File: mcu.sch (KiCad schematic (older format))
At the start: 26 parts, among them SW1 PTS645VL39-2, U4 CAT24C32, U5 STM32F765VIT6, X1 ECS-TXO-3225-160-TR

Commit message: Complete functional design
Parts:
- renumbered C16 to C15, C17 to C16, C18 to C17, C19 to C18, C20 to C19, C21 to C20, C22 to C21, C23 to C22, C24 to C23, C25 to C24, C26 to C25, C27 to C26, C28 to C27, C29 to C28, D33 to D6, R7 to R10, R8 to R11, R9 to R12, R125 to R9
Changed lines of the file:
@@
 $EndDescr
 $Comp
-L Device:R R9
+L Device:R R12
 U 1 1 5AD0B119
 P 10200 5950
-F 0 "R9" H 10000 5900 50  0000 L CNN
+F 0 "R12" H 10000 5900 50  0000 L CNN
 F 1 "47k" H 10000 6000 50  0000 L CNN
 F 2 "Resistor_SMD:R_0603_1608Metric" V 10130 5950 50  0001 C CNN
@@
 VDD3V3
 $Comp
-L Device:C C20
+L Device:C C19
 U 1 1 5AD085F7
 P 1800 6650
-F 0 "C20" H 1915 6696 50  0000 L CNN
+F 0 "C19" H 1915 6696 50  0000 L CNN
 F 1 "1uF" H 1915 6605 50  0000 L CNN
 F 2 "Capacitor_SMD:C_0603_1608Metric" H 1838 6500 50  0001 C CNN
@@
 $EndComp
 $Comp
-L Device:C C24
+L Device:C C23
 U 1 1 5AD086E9
 P 2200 6650
-F 0 "C24" H 2315 6696 50  0000 L CNN
+F 0 "C23" H 2315 6696 50  0000 L CNN
 F 1 "100nF" H 2315 6605 50  0000 L CNN
 F 2 "Capacitor_SMD:C_0603_1608Metric" H 2238 6500 50  0001 C CNN
@@
 VDD3V3
 $Comp
-L Device:C C19
+L Device:C C18
 U 1 1 5AD08A76
 P 1800 6250
-F 0 "C19" H 1915 6296 50  0000 L CNN
+F 0 "C18" H 1915 6296 50  0000 L CNN
 F 1 "1uF" H 1915 6205 50  0000 L CNN
 F 2 "Capacitor_SMD:C_0603_1608Metric" H 1838 6100 50  0001 C CNN
@@
 $EndComp
 $Comp
-L Device:C C23
+L Device:C C22
 U 1 1 5AD08A7D
 P 2200 6250
-F 0 "C23" H 2315 6296 50  0000 L CNN
+F 0 "C22" H 2315 6296 50  0000 L CNN
 F 1 "100nF" H 2315 6205 50  0000 L CNN
 F 2 "Capacitor_SMD:C_0603_1608Metric" H 2238 6100 50  0001 C CNN
@@
 VDD3V3
 $Comp
-L Device:C C16
+L Device:C C15
 U 1 1 5AD0945E
 P 1150 7300
-F 0 "C16" H 1265 7346 50  0000 L CNN
+F 0 "C15" H 1265 7346 50  0000 L CNN
 F 1 "100nF" H 1265 7255 50  0000 L CNN
 F 2 "Capacitor_SMD:C_0603_1608Metric" H 1188 7150 50  0001 C CNN
@@
 $EndComp
 $Comp
-L Device:C C17
+L Device:C C16
 U 1 1 5AD09C8C
 P 1600 7300
-F 0 "C17" H 1715 7346 50  0000 L CNN
+F 0 "C16" H 1715 7346 50  0000 L CNN
 F 1 "100nF" H 1715 7255 50  0000 L CNN
 F 2 "Capacitor_SMD:C_0603_1608Metric" H 1638 7150 50  0001 C CNN
@@
 $EndComp
 $Comp
-L Device:C C22
+L Device:C C21
 U 1 1 5AD09D94
 P 2050 7300
-F 0 "C22" H 2165 7346 50  0000 L CNN
+F 0 "C21" H 2165 7346 50  0000 L CNN
 F 1 "100nF" H 2165 7255 50  0000 L CNN
 F 2 "Capacitor_SMD:C_0603_1608Metric" H 2088 7150 50  0001 C CNN
@@
 $EndComp
 $Comp
-L Device:C C25
+L Device:C C24
 U 1 1 5AD09D9B
 P 2500 7300
-F 0 "C25" H 2615 7346 50  0000 L CNN
+F 0 "C24" H 2615 7346 50  0000 L CNN
 F 1 "100nF" H 2615 7255 50  0000 L CNN
 F 2 "Capacitor_SMD:C_0603_1608Metric" H 2538 7150 50  0001 C CNN
@@
 $EndComp
 $Comp
-L Device:C C26
+L Device:C C25
 U 1 1 5AD09E94
 P 2950 7300
-F 0 "C26" H 3065 7346 50  0000 L CNN
+F 0 "C25" H 3065 7346 50  0000 L CNN
 F 1 "100nF" H 3065 7255 50  0000 L CNN
 F 2 "Capacitor_SMD:C_0603_1608Metric" H 2988 7150 50  0001 C CNN
@@
 VDD3V3
 $Comp
-L Device:C C27
+L Device:C C26
 U 1 1 5AD0FCE6
 P 3250 6450
-F 0 "C27" H 3400 6450 50  0000 L CNN
+F 0 "C26" H 3400 6450 50  0000 L CNN
 F 1 "2.2uF" H 3350 6550 50  0000 L CNN
 F 2 "Capacitor_SMD:C_0603_1608Metric" H 3288 6300 50  0001 C CNN
@@
 $EndComp
 $Comp
-L Device:C C29
+L Device:C C28
 U 1 1 5AD117D1
 P 3650 6450
-F 0 "C29" H 3400 6450 50  0000 L CNN
+F 0 "C28" H 3400 6450 50  0000 L CNN
 F 1 "2.2uF" H 3350 6550 50  0000 L CNN
 F 2 "Capacitor_SMD:C_0603_1608Metric" H 3688 6300 50  0001 C CNN
@@
 $EndComp
 $Comp
-L power:GND #PWR041
+L power:GND #PWR042
 U 1 1 5AF5CFF3
 P 5650 850
-F 0 "#PWR041" H 5650 600 50  0001 C CNN
+F 0 "#PWR042" H 5650 600 50  0001 C CNN
 F 1 "GND" H 5655 677 50  0000 C CNN
 F 2 "" H 5650 850 50  0001 C CNN
@@
 $EndComp
 $Comp
-L power:GND #PWR043
+L power:GND #PWR044
 U 1 1 5AF5E7FC
 P 9300 1900
-F 0 "#PWR043" H 9300 1650 50  0001 C CNN
+F 0 "#PWR044" H 9300 1650 50  0001 C CNN
 F 1 "GND" H 9300 1750 50  0000 C CNN
 F 2 "" H 9300 1900 50  0001 C CNN
@@
 $EndComp
 $Comp
-L power:GND #PWR042
+L power:GND #PWR043
 U 1 1 5AF5F2E4
 P 7850 5200
-F 0 "#PWR042" H 7850 4950 50  0001 C CNN
+F 0 "#PWR043" H 7850 4950 50  0001 C CNN
 F 1 "GND" H 7855 5027 50  0000 C CNN
 F 2 "" H 7850 5200 50  0001 C CNN
@@
 	1500 2700 1750 2700
 $Comp
-L Device:C C21
+L Device:C C20
 U 1 1 5AF62329
 P 1950 3050
-F 0 "C21" V 2202 3050 50  0000 C CNN
+F 0 "C20" V 2202 3050 50  0000 C CNN
 F 1 "100nF" V 2111 3050 50  0000 C CNN
 F 2 "Capacitor_SMD:C_0603_1608Metric" H 1988 2900 50  0001 C CNN
@@
 	1500 3050 1800 3050
 $Comp
-L power:GND #PWR044
+L power:GND #PWR045
 U 1 1 5AF66D47
 P 10450 5700
-F 0 "#PWR044" H 10450 5450 50  0001 C CNN
+F 0 "#PWR045" H 10450 5450 50  0001 C CNN
 F 1 "GND" H 10455 5527 50  0000 C CNN
 F 2 "" H 10450 5700 50  0001 C CNN
@@
 $EndComp
 $Comp
-L Device:C C18
+L Device:C C17
 U 1 1 5BC55501
 P 1700 1500
-F 0 "C18" H 1450 1550 50  0000 C CNN
+F 0 "C17" H 1450 1550 50  0000 C CNN
 F 1 "100nF" H 1450 1450 50  0000 C CNN
 F 2 "Capacitor_SMD:C_0603_1608Metric" H 1738 1350 50  0001 C CNN
@@
 VDD3V3
 $Comp
-L Device:C C28
+L Device:C C27
 U 1 1 5BC224AB
 P 3400 7300
-F 0 "C28" H 3515 7346 50  0000 L CNN
+F 0 "C27" H 3515 7346 50  0000 L CNN
 F 1 "100nF" H 3515 7255 50  0000 L CNN
 F 2 "Capacitor_SMD:C_0603_1608Metric" H 3438 7150 50  0001 C CNN
@@
 BOOT
 $Comp
-L Device:R R7
+L Device:R R10
 U 1 1 5BCD0D7A
 P 9600 5950
-F 0 "R7" H 9400 5900 50  0000 L CNN
+F 0 "R10" H 9400 5900 50  0000 L CNN
 F 1 "4.7k" H 9400 6000 50  0000 L CNN
 F 2 "Resistor_SMD:R_0603_1608Metric" V 9530 5950 50  0001 C CNN
@@
 VDD3V3
 $Comp
-L Device:R R8
+L Device:R R11
 U 1 1 5BCDCE1E
 P 9900 5950
-F 0 "R8" H 9700 5900 50  0000 L CNN
+F 0 "R11" H 9700 5900 50  0000 L CNN
 F 1 "4.7k" H 9700 6000 50  0000 L CNN
 F 2 "Resistor_SMD:R_0603_1608Metric" V 9830 5950 50  0001 C CNN
@@
 P 5550 6250
 AR Path="/5BC54251/5BCE7FB5" Ref="R?"  Part="1"
-AR Path="/5BC1C8A4/5BCE7FB5" Ref="R125"  Part="1"
-F 0 "R125" H 5620 6296 50  0000 L CNN
+AR Path="/5BC1C8A4/5BCE7FB5" Ref="R9"  Part="1"
+F 0 "R9" H 5620 6296 50  0000 L CNN
 F 1 "1k" H 5620 6205 50  0000 L CNN
 F 2 "Resistor_SMD:R_0603_1608Metric" V 5480 6250 50  0001 C CNN
@@
 P 5550 6550
 AR Path="/5BC54251/5BCE7FBC" Ref="D?"  Part="1"
-AR Path="/5BC1C8A4/5BCE7FBC" Ref="D33"  Part="1"
-F 0 "D33" V 5588 6433 50  0000 R CNN
+AR Path="/5BC1C8A4/5BCE7FBC" Ref="D6"  Part="1"
+F 0 "D6" V 5588 6433 50  0000 R CNN
 F 1 "LTST-C194KSKT" V 5497 6433 50  0000 R CNN
 F 2 "LED_SMD:LED_0603_1608Metric" H 5550 6550 50  0001 C CNN
@@
 $EndComp
 $Comp
-L power:GND #PWR0131
+L power:GND #PWR041
 U 1 1 5BCEB458
 P 5550 6700
-F 0 "#PWR0131" H 5550 6450 50  0001 C CNN
+F 0 "#PWR041" H 5550 6450 50  0001 C CNN
 F 1 "GND" H 5555 6527 50  0000 C CNN
 F 2 "" H 5550 6700 50  0001 C CNN

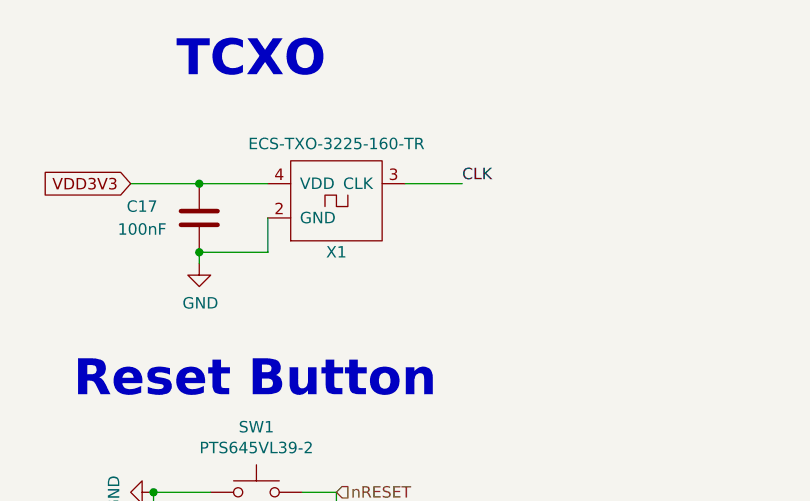
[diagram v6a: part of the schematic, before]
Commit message: Finish silkscreen and updated README.md
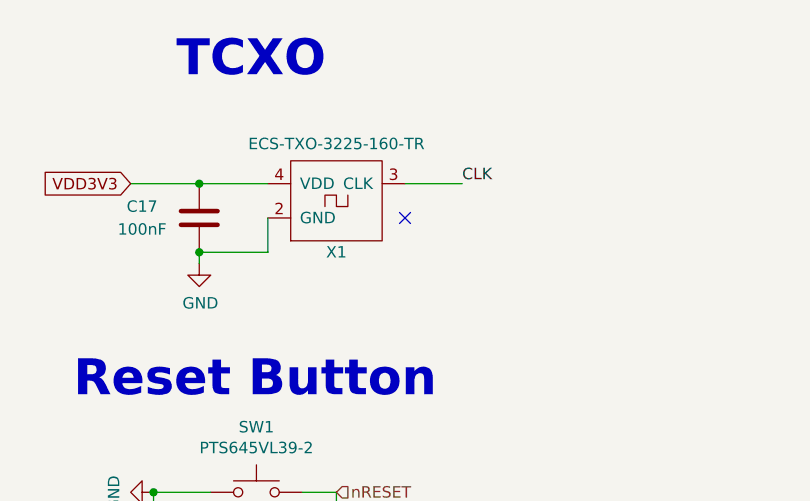
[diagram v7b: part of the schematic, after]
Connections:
- no-connect marks 24 -> 25
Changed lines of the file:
@@
 	1    0    0    -1
 $EndComp
+NoConn ~ 2600 1500
 $EndSCHEMATC
